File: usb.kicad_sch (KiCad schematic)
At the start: 6 parts, among them J1 GSB1C211110DS1HR, U1 TPS7B8133DRVR

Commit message: completed 0.1 schematic design
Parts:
- C1, C2: footprint (none) -> Capacitor_SMD:C_0603_1608Metric
- J1: value GSB1C211110DS1HR -> USB4085-GF-A; footprint (none) -> Connector_USB:USB_C_Receptacle_GCT_USB4085
- R1, R2: footprint (none) -> Resistor_SMD:R_0402_1005Metric

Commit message: re-done whole pcb
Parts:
- J1: value USB4085-GF-A -> GSB1C411111DS1HR; footprint Connector_USB:USB_C_Receptacle_GCT_USB4085 -> usb_personal:AMPHENOL_GSB1C411111DS1HR
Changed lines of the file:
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@@
 			)
 		)
-		(property "Value" "USB4085-GF-A"
+		(property "Value" "GSB1C411111DS1HR"
 			(at 95.25 76.2 0)
 			(effects
@@
 			)
 		)
-		(property "Footprint" "Connector_USB:USB_C_Receptacle_GCT_USB4085"
+		(property "Footprint" "usb_personal:AMPHENOL_GSB1C411111DS1HR"
 			(at 99.06 96.52 0)
 			(effects
@@
 			)
 		)
-		(property "Description" "USB 2.0-only 16P Type-C Receptacle connector"
+		(property "Description" ""
 			(at 95.25 96.52 0)
 			(effects

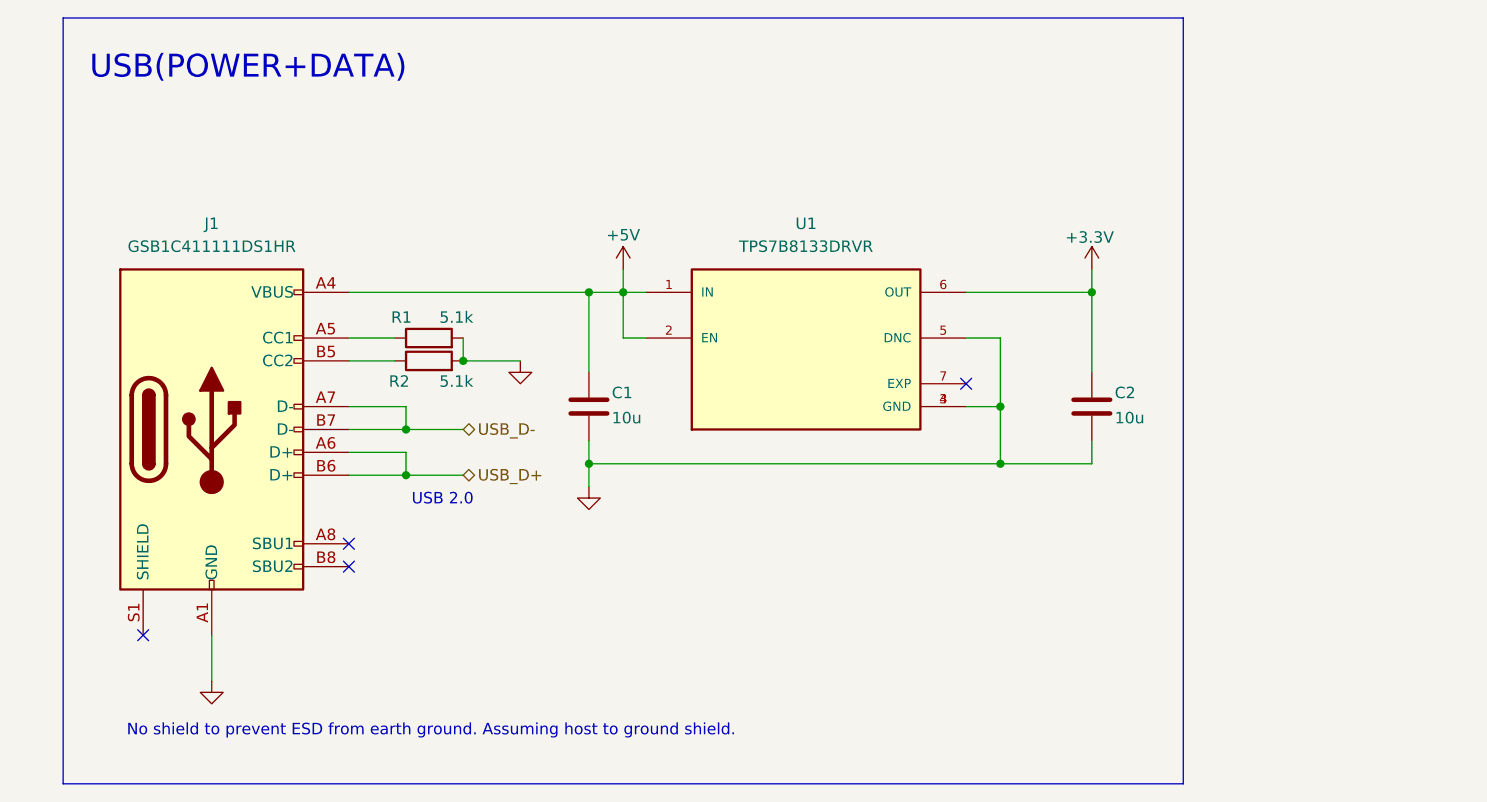
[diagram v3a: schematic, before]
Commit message: added ESD protection, re-wired matrix
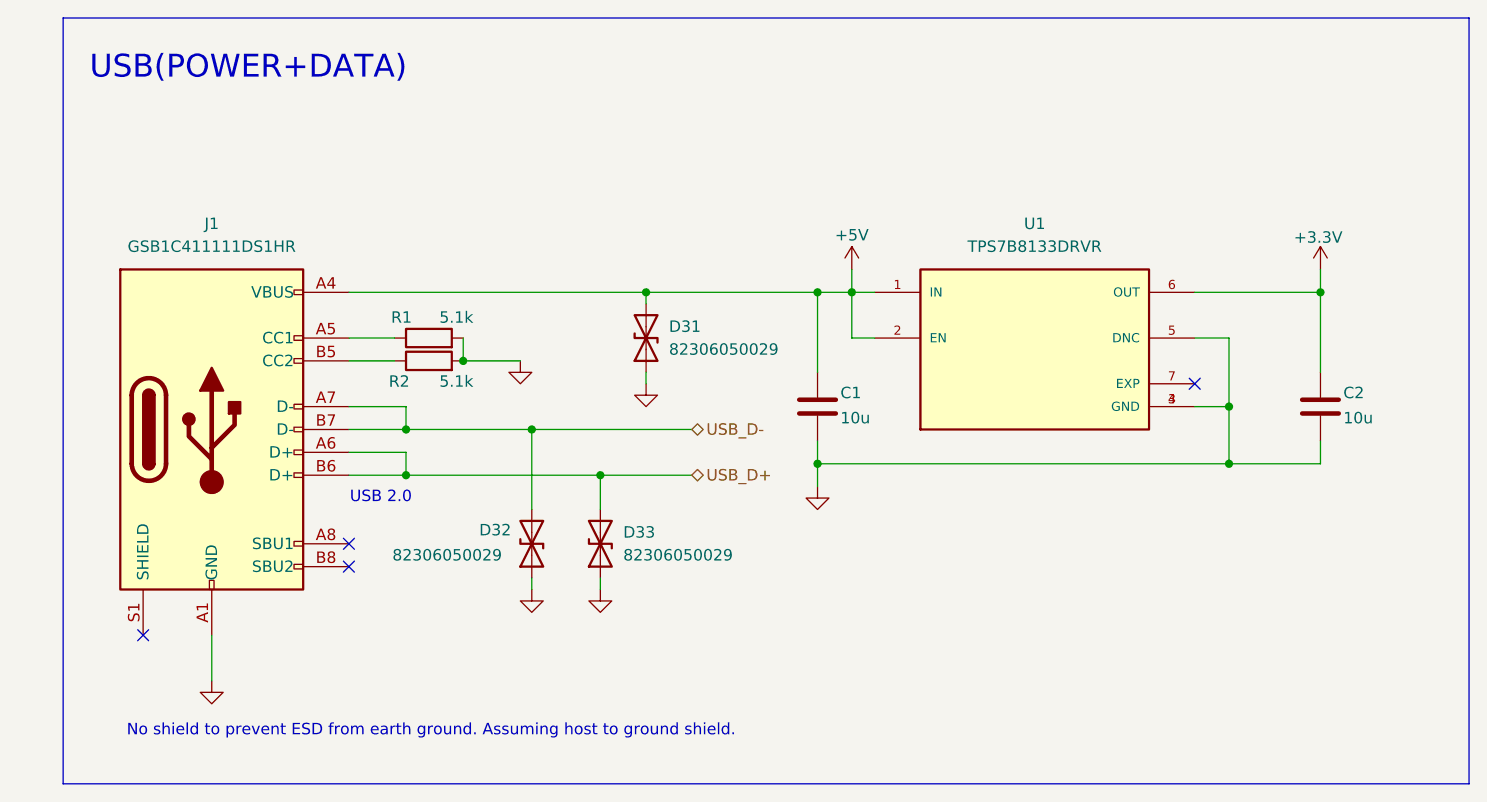
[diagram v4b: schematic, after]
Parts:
- added D31, D32, D33: 82306050029, Diode_SMD:D_0603_1608Metric, symbol Device:D_TVS
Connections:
- net +5V: now also D31.2 (A2)
- net GND: now also D31.1 (A1), D32.1 (A1), D33.1 (A1)
- net USB_D+: now also D33.2 (A2)
- net USB_D-: now also D32.2 (A2)
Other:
- moved on the sheet: C1, C2, U1
